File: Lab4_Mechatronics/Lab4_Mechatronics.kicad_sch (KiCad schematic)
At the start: 8 parts

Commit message: added lab 4 schematic
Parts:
- added D1, D2, D3: 1N5819, Diode_THT:D_DO-41_SOD81_P10.16mm_Horizontal, symbol Diode:1N5819
- added Q1: Open_Drain, symbol Simulation_SPICE:NMOS
- added R4, R6, R7: 1Meg, symbol Device:R_US
- added R5, R9: 10k, symbol Device:R_US
- added R8: 47k, symbol Device:R_US
- added Tiva_Voltage_Source (x2): 5V, symbol Simulation_SPICE:VDC
- added Tiva_Voltage_Source: 5, symbol Simulation_SPICE:VDC
- added U1: LM311, symbol Comparator:LM311
- added V3: 6V, symbol Simulation_SPICE:VDC
- High_Power_Voltage_Source: value 6 -> 6V
- Tiva_Power_Source: value 5V or 3.3V -> 5V
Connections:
- net GND: now also D2.2 (A), D3.2 (A), Q1.3 (S), Tiva_Voltage_Source.2, Tiva_Voltage_Source.2, Tiva_Voltage_Source.2, U1.1 (GND), U1.4 (V-), V3.2
- net at R2.1: now also L3.1
- net Coil_B: now reaches R2.2
- net Coil_B: now also R4.2
- net at L3.2: now also L1.1, L2.1
- net at L1.2: now also R3.1
- net Coil_C: now reaches R3.2
- net Coil_C: now also R6.2
- net at L2.2: now also R1.1
- net Coil_A: now reaches R1.2
- net Coil_A: now also R7.2
- new net: R9.2, Tiva_Voltage_Source.1
- new net: D1.2 (A), D2.1 (K), R8.2, U1.2 (+)
- new net: R5.1, Tiva_Voltage_Source.1
- new net Brown/Blue/Orange_Port: Q1.1 (D), R5.2, R9.1, U1.7
- new net Coil_A/B/C: R8.1
- new net Virtual Common(White Port): R4.1, R6.1, R7.1
- new net Virtual_Common(White_Port): D1.1 (K), D3.1 (K), U1.3 (-), U1.8 (V+), V3.1
- new net Yellow: Tiva_Voltage_Source.1
- no-connect marks 12 -> 17
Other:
- note added: "+ + + + +"
- note added: "- - - - -"
- note added: "N"
- note added: "S"
- moved on the sheet: High_Power_Voltage_Source, Tiva_Power_Source

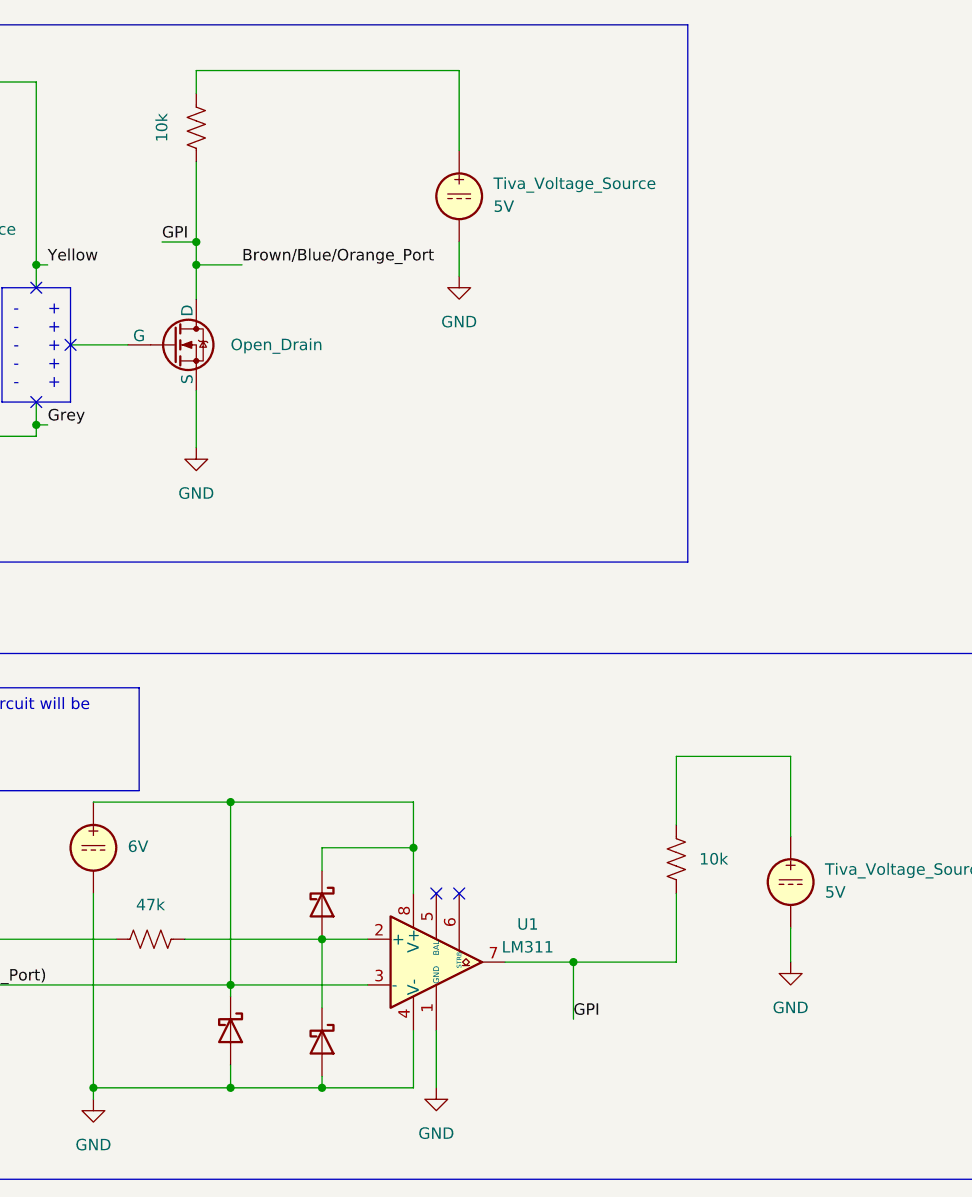
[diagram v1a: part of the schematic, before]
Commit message: added lab 5 schematic
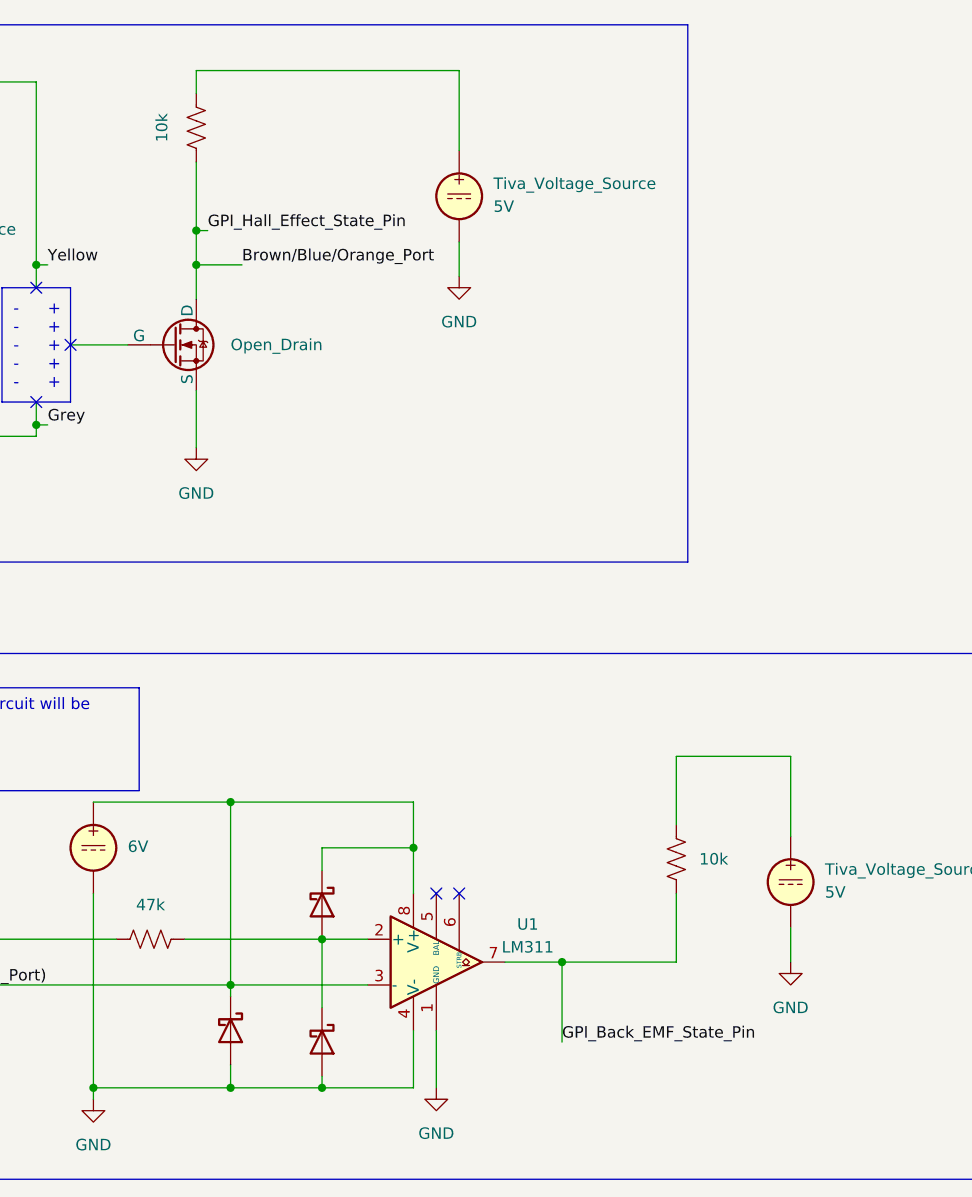
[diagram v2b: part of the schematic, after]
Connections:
- net Brown/Blue/Orange_Port: no longer R9.1, U1.7
- new net GPI_Back_EMF_State_Pin: R9.1, U1.7
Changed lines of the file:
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@@
   (junction (at 93.98 243.84) (diameter 0) (color 0 0 0 0)
   )
+  (junction (at 120.65 246.38) (diameter 0) (color 0 0 0 0)
+  )
   (junction (at 62.23 168.91) (diameter 0) (color 175 166 46 1)
   )
@@
   (junction (at 68.58 260.35) (diameter 0) (color 0 0 0 0)
   )
-  (junction (at 121.92 246.38) (diameter 0) (color 0 0 0 0)
-  )
-  (junction (at 80.01 166.37) (diameter 0) (color 0 0 0 0)
+  (junction (at 80.01 165.1) (diameter 0) (color 0 0 0 0)
   )
   (no_connect (at 62.23 184.15))
@@
     (stroke (width 0) (type default))
   )
-  (wire (pts (xy 114.3 246.38) (xy 121.92 246.38))
+  (wire (pts (xy 114.3 246.38) (xy 120.65 246.38))
     (stroke (width 0) (type default))
   )
@@
     (stroke (width 0) (type default))
   )
-  (wire (pts (xy 80.01 166.37) (xy 80.01 168.91))
+  (wire (pts (xy 80.01 165.1) (xy 80.01 168.91))
     (stroke (width 0) (type default))
   )
@@
     (stroke (width 0) (type default))
   )
-  (wire (pts (xy 121.92 246.38) (xy 133.35 246.38))
-    (stroke (width 0) (type default))
-  )
   (wire (pts (xy 280.67 99.06) (xy 262.89 99.06))
     (stroke (width 0) (type default))
@@
     (stroke (width 0) (type default))
   )
-  (wire (pts (xy 76.2 166.37) (xy 80.01 166.37))
+  (wire (pts (xy 81.28 165.1) (xy 80.01 165.1))
     (stroke (width 0) (type default))
   )
@@
     (stroke (width 0) (type default))
   )
-  (wire (pts (xy 121.92 246.38) (xy 121.92 252.73))
+  (wire (pts (xy 120.65 246.38) (xy 120.65 255.27))
     (stroke (width 0) (type default))
   )
@@
     (stroke (width 0) (type default))
   )
-  (wire (pts (xy 80.01 157.48) (xy 80.01 166.37))
+  (wire (pts (xy 80.01 157.48) (xy 80.01 165.1))
     (stroke (width 0) (type default))
   )
@@
   )
   (wire (pts (xy 280.67 99.06) (xy 280.67 110.49))
+    (stroke (width 0) (type default))
+  )
+  (wire (pts (xy 120.65 246.38) (xy 133.35 246.38))
     (stroke (width 0) (type default))
   )
@@
     (effects (font (size 1.27 1.27)) (justify left bottom))
   )
-  (label "GPI" (at 121.92 252.73 0) (fields_autoplaced)
+  (label "GPI_Back_EMF_State_Pin" (at 120.65 255.27 0) (fields_autoplaced)
     (effects (font (size 1.27 1.27)) (justify left bottom))
   )
@@
     (effects (font (size 1.27 1.27)) (justify left bottom))
   )
-  (label "GPI" (at 76.2 166.37 0) (fields_autoplaced)
-    (effects (font (size 1.27 1.27)) (justify left bottom))
-  )
+  (label "GPI_Hall_Effect_State_Pin" (at 81.28 165.1 0) (fields_autoplaced)
+    (effects (font (size 1.27 1.27)) (justify left bottom))
+  )
